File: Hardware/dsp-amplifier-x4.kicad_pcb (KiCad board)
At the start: 4 copper layers, 182 x 90 mm, 171 parts, among them J1 USBi, J10 Conn_Coaxial, J2 EXT, J3 Raspberry_Pi_2_3, J4 Screw_Terminal_01x02, J5 Screw_Terminal_01x02, J6 Screw_Terminal_01x02, J7 Screw_Terminal_01x02, J8 USB_B, J9 Conn_Coaxial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

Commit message: smallify
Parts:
- removed C28, C32: 100n, Capacitor_SMD:C_0603_1608Metric_Pad1.08x0.95mm_HandSolder
- removed C30, C34, C36, C38, C40: 10u, Capacitor_SMD:C_1206_3216Metric_Pad1.33x1.80mm_HandSolder
- removed L1: 10u, Inductor_SMD:L_Abracon_ASPI-0630LR
- removed R25: 511k, Resistor_SMD:R_0603_1608Metric_Pad0.98x0.95mm_HandSolder
- removed R26, R29: 100k, Resistor_SMD:R_0603_1608Metric_Pad0.98x0.95mm_HandSolder
- removed R30: 13.5k, Resistor_SMD:R_0603_1608Metric_Pad0.98x0.95mm_HandSolder
- removed U3: TPS54308, Package_TO_SOT_SMD:SOT-23-6
- moved U5 107.7 mm to (125.8, 49.8)
- moved C42 94.7 mm to (133.0, 51.0), turned to 0 degrees
- moved C37 71.6 mm to (139.5, 71.2), turned to 90 degrees
- moved C41 67.9 mm to (142.2, 71.2), turned to 90 degrees
- moved L2 66.1 mm to (146.5, 78.0), turned to 0 degrees
- moved C35 64.2 mm to (145.0, 71.2), turned to 90 degrees
- moved C39 60.5 mm to (147.8, 71.2), turned to 90 degrees
- moved C33 53.3 mm to (149.2, 66.5), turned to 90 degrees
- moved C29 52.9 mm to (153.5, 73.0), turned to 180 degrees
- moved U4 51.2 mm to (152.0, 66.5), turned to 90 degrees
- moved C31 49.9 mm to (154.0, 75.2), turned to 180 degrees
- moved R32 49.0 mm to (152.0, 63.5), turned to 180 degrees
- moved R31 48.6 mm to (152.0, 61.8), turned to 0 degrees
- moved R27 47.3 mm to (154.8, 66.5), turned to 90 degrees
- moved R28 46.1 mm to (154.8, 63.0), turned to 90 degrees
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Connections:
- J3 pad 2: +5VD -> +5VA
- J3 pad 4: +5VD -> +5VA
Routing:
- net +5VA: track 225.4 -> 26.2 mm, vias 5 -> 0
- net +5VD: track 27.4 -> 0.00 mm, vias 6 -> 0
- net GND: track 218.5 -> 192.1 mm, vias 114 -> 88
- net /PI_SDATA_O: track 72.8 -> 65.6 mm
- net Net-(C32-Pad1): track 7.00 -> 0.00 mm, vias 9 -> 0
- net Net-(R25-Pad2): track 5.96 -> 0.00 mm
- net /Power/FB_5V0: track 5.17 -> 0.00 mm
- net Net-(J3-Pad40): track 6.33 -> 10.9 mm
- net Net-(C32-Pad2): track 3.57 -> 0.00 mm
- net Net-(C33-Pad1): track 7.00 -> 3.91 mm, vias 9 -> 7
- net /PI_LRCLK: track 67.1 -> 64.3 mm
- net Net-(C33-Pad2): track 3.57 -> 1.90 mm
- net /Power/FB_5V0_SEC: track 5.17 -> 3.67 mm
- net +3.3VA: vias 18 -> 6
- added copper zone on In2.Cu, net +5VA
- removed copper zone on F.Cu, net +3.3VA
- removed copper zone on In2.Cu, net +3.3VA
- removed copper zone on F.Cu, net +5VD
- removed copper zone on In2.Cu, net +5VD
- removed copper zone on B.Cu, net Net-(C32-Pad1)
- removed copper zone on F.Cu, net Net-(C32-Pad1)
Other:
- board text added: "+5V"
- board text added: "+5V supplied"
- board text removed: "+3.3VA"
- board text removed: "+5VA"
- board text removed: "+5VA supplied"
- board text removed: "+5VD"
- board text removed: "DC/DC"

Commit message: slight adjustments
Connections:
- J3 pad 13: /PI_MUTE -> (no net)
- U1 pad 69: /PI_MUTE -> (no net)
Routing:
- net /PI_MUTE: track 58.1 -> 0.00 mm, vias 2 -> 0
- net (no net): track 0.00 -> 58.1 mm, vias 6 -> 8

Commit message: mostly ready
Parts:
- removed P1: Conn_WallPlug, terminal_connectors:wuerth_691216410002
- removed PS1: IRM-60-24, Converter_ACDC:Converter_ACDC_MeanWell_IRM-60-xx_THT
- added J11: Screw_Terminal_01x02, terminal_connectors:wuerth_691216410002, B.Cu at (172.0, 71.5)
- moved C42 17.0 mm to (123.0, 64.8), turned to 270 degrees
- moved U5 14.7 mm to (129.2, 64.0), turned to 180 degrees
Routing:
- net +5VA: track 26.2 -> 110.9 mm, vias 0 -> 13
- net /Power/AC_N: track 33.8 -> 0.00 mm
- net /Power/AC_L: track 21.7 -> 0.00 mm
- net GND: track 192.1 -> 192.4 mm, vias 88 -> 91
- net +3.3VA: vias 6 -> 10
- net (no net): vias 8 -> 6
- added copper zone on F.Cu, net +3.3VA
- added copper zone on In2.Cu, net +3.3VA
- removed copper zone on In2.Cu, net +24V
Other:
- board size 182 x 90 mm -> 121.2 x 90 mm
- board text removed: "!"
- board text removed: "0/0"
- board text removed: "0/80"
- board text removed: "108/76"
- board text removed: "172/0"
- board text removed: "172/80"
- board text removed: "80/0"
- board text removed: "AC"

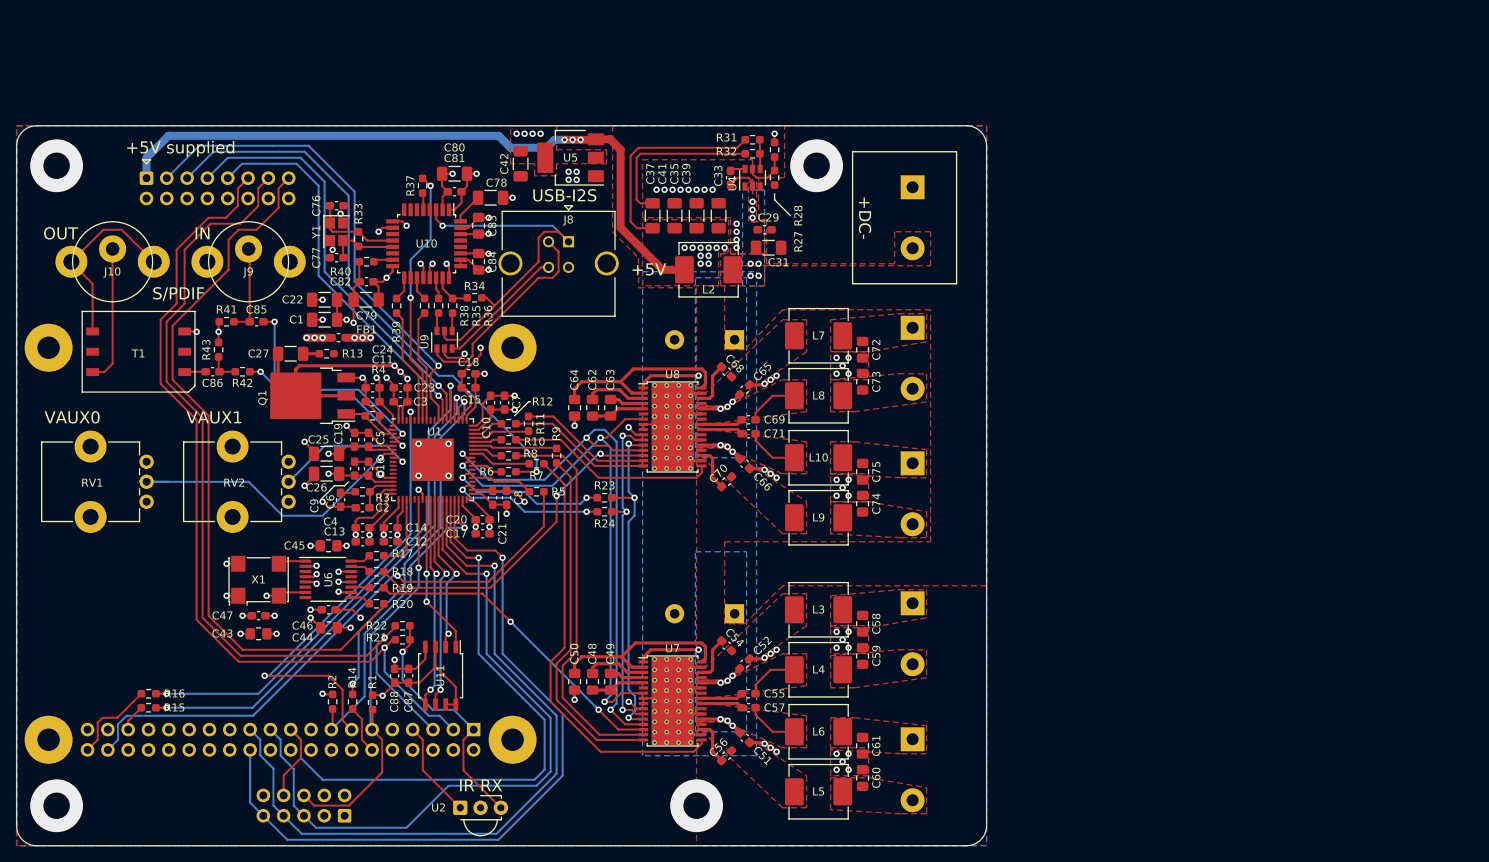
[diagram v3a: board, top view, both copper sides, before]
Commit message: feat: finalize layout for smaller blus
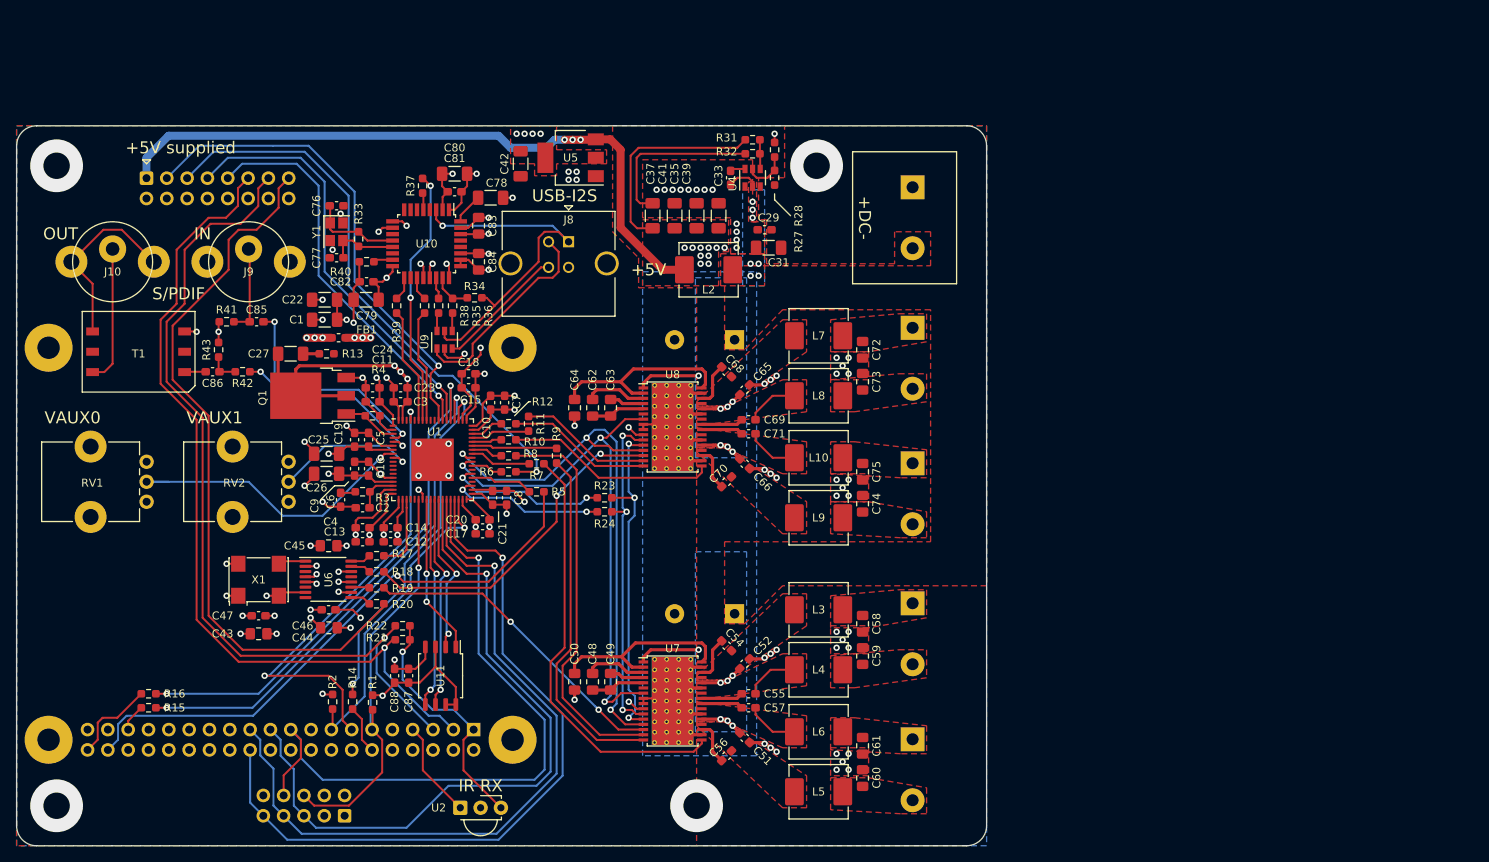
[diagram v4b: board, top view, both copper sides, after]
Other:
- net class Default removed
- board text added: "schwergängige poti montageöffnungen"

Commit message: Updated power supply
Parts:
- removed C37, C39, C41, C42: 10u, Capacitor_SMD:C_1206_3216Metric_Pad1.33x1.80mm_HandSolder
- removed L2: 10u, Inductor_SMD:L_Abracon_ASPI-0630LR
- removed R27: 511k, Resistor_SMD:R_0603_1608Metric_Pad0.98x0.95mm_HandSolder
- removed R28, R31: 100k, Resistor_SMD:R_0603_1608Metric_Pad0.98x0.95mm_HandSolder
- removed R32: 13.5k, Resistor_SMD:R_0603_1608Metric_Pad0.98x0.95mm_HandSolder
- removed U5: AMS1117-3.3, Package_TO_SOT_SMD:SOT-223-3_TabPin2
- added C28: 100n, Capacitor_SMD:C_0603_1608Metric_Pad1.08x0.95mm_HandSolder, F.Cu at (146.8, 74.0)
- added C30: 100n, Capacitor_SMD:C_0603_1608Metric_Pad1.08x0.95mm_HandSolder, F.Cu at (151.5, 71.2)
- added C32: 10u, Capacitor_SMD:C_1206_3216Metric_Pad1.33x1.80mm_HandSolder, F.Cu at (146.0, 65.0)
- added C34: 10u, Capacitor_SMD:C_1206_3216Metric_Pad1.33x1.80mm_HandSolder, F.Cu at (146.0, 62.5)
- added L1: 4.7u, Inductor_SMD:L_Abracon_ASPI-0630LR, F.Cu at (139.8, 71.0)
- added R25: 54.9k, Resistor_SMD:R_0603_1608Metric_Pad0.98x0.95mm_HandSolder, F.Cu at (154.6, 74.0)
- added R26: 10k, Resistor_SMD:R_0603_1608Metric_Pad0.98x0.95mm_HandSolder, F.Cu at (156.4, 74.0)
- added U3: TPS563200, Package_TO_SOT_SMD:SOT-23-6, F.Cu at (151.5, 74.0)
- C29, C33: value 100n -> 10u; footprint Capacitor_SMD:C_0603_1608Metric_Pad1.08x0.95mm_HandSolder -> Capacitor_SMD:C_1206_3216Metric_Pad1.33x1.80mm_HandSolder
- J11: moved to F.Cu
- U4: value TPS54308 -> AMS1117-3.3; footprint Package_TO_SOT_SMD:SOT-23-6 -> Package_TO_SOT_SMD:SOT-223-3_TabPin2
- moved C35 24.7 mm to (121.5, 63.5), turned to 180 degrees
- moved U4 22.9 mm to (129.2, 64.0), turned to 180 degrees
- moved C31 9.57 mm to (146.0, 70.0), turned to 0 degrees
- moved C29 8.81 mm to (144.8, 74.0), turned to 90 degrees
- moved C33 3.40 mm to (146.0, 67.5), turned to 0 degrees
- moved J11 0.06 mm to (172.0, 71.6)
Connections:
- C29 pad 1: +24V -> +15V
- C31 pad 1: +24V -> +5VA
- C33 pad 1: Net-(C33-Pad1) -> +5VA
- C33 pad 2: Net-(C33-Pad2) -> GND
- C35 pad 1: +5VA -> +3.3VA
- C51 pad 1: +24V -> +15V
- C52 pad 1: +24V -> +15V
- C53 pad 1: +24V -> +15V
- C65 pad 1: +24V -> +15V
- C66 pad 1: +24V -> +15V
- C67 pad 1: +24V -> +15V
- J1 pad 1: (no net) -> unconnected-(J1-Pad1)
- J1 pad 2: (no net) -> unconnected-(J1-Pad2)
- J1 pad 3: (no net) -> unconnected-(J1-Pad3)
- J1 pad 4: (no net) -> unconnected-(J1-Pad4)
- J11 pad 1: +24V -> +15V
- J3 pad 10: (no net) -> unconnected-(J3-Pad10)
- J3 pad 13: (no net) -> unconnected-(J3-Pad13)
- J3 pad 16: (no net) -> unconnected-(J3-Pad16)
- J3 pad 17: (no net) -> unconnected-(J3-Pad17)
- J3 pad 18: (no net) -> unconnected-(J3-Pad18)
- J3 pad 22: (no net) -> unconnected-(J3-Pad22)
- J3 pad 26: (no net) -> unconnected-(J3-Pad26)
- J3 pad 27: (no net) -> unconnected-(J3-Pad27)
- J3 pad 28: (no net) -> unconnected-(J3-Pad28)
- J3 pad 29: (no net) -> unconnected-(J3-Pad29)
- J3 pad 31: (no net) -> unconnected-(J3-Pad31)
- J3 pad 32: (no net) -> unconnected-(J3-Pad32)
- J3 pad 33: (no net) -> unconnected-(J3-Pad33)
- J3 pad 36: (no net) -> unconnected-(J3-Pad36)
- J3 pad 37: (no net) -> unconnected-(J3-Pad37)
- J3 pad 8: (no net) -> unconnected-(J3-Pad8)
- T1 pad 2: (no net) -> unconnected-(T1-Pad2)
- T1 pad 5: (no net) -> unconnected-(T1-Pad5)
- U1 pad 10: (no net) -> unconnected-(U1-Pad10)
- U1 pad 11: (no net) -> unconnected-(U1-Pad11)
- U1 pad 12: (no net) -> unconnected-(U1-Pad12)
- U1 pad 13: (no net) -> unconnected-(U1-Pad13)
- U1 pad 22: (no net) -> unconnected-(U1-Pad22)
- U1 pad 23: (no net) -> unconnected-(U1-Pad23)
- U1 pad 40: (no net) -> unconnected-(U1-Pad40)
- U1 pad 43: (no net) -> unconnected-(U1-Pad43)
- U1 pad 63: (no net) -> unconnected-(U1-Pad63)
- U1 pad 64: (no net) -> unconnected-(U1-Pad64)
- U1 pad 68: (no net) -> /AUX_BCLK
- U1 pad 69: (no net) -> /AUX_LRCLK
- U1 pad 70: (no net) -> /AUX_MDI
- U10 pad 11: (no net) -> /USB_SUSPEND
- U10 pad 14: (no net) -> unconnected-(U10-Pad14)
- U10 pad 18: (no net) -> unconnected-(U10-Pad18)
- U10 pad 28: (no net) -> unconnected-(U10-Pad28)
- U10 pad 29: (no net) -> unconnected-(U10-Pad29)
- U10 pad 4: (no net) -> unconnected-(U10-Pad4)
- U10 pad 6: (no net) -> unconnected-(U10-Pad6)
- U10 pad 7: (no net) -> unconnected-(U10-Pad7)
- U10 pad 8: (no net) -> unconnected-(U10-Pad8)
- U4 pad 2: Net-(C33-Pad1) -> +3.3VA
- U4 pad 3: +24V -> +5VA
- U6 pad 13: (no net) -> /Clock/CLK2
- U6 pad 3: (no net) -> /Clock/CLK0
- U6 pad 6: (no net) -> /Clock/CLK4
- U6 pad 8: (no net) -> /Clock/CLK6
- U7 pad 1: +24V -> +15V
- U7 pad 21: +24V -> +15V
- U7 pad 28: +24V -> +15V
- U7 pad 6: (no net) -> /I2S-AMP-2CH-A/NSPK_FAULT
- U8 pad 1: +24V -> +15V
- U8 pad 21: +24V -> +15V
- U8 pad 28: +24V -> +15V
- U8 pad 6: (no net) -> /I2S-AMP-2CH-B/NSPK_FAULT
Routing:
- net unconnected-(J3-Pad13): track 0.00 -> 58.1 mm, vias 0 -> 2
- net (no net): track 58.1 -> 0.00 mm, vias 6 -> 4
- net +24V: track 37.6 -> 0.00 mm, vias 14 -> 0
- net +15V: track 0.00 -> 37.6 mm, vias 0 -> 14
- net +5VA: track 110.9 -> 82.2 mm, vias 13 -> 3
- net GND: track 192.4 -> 173.8 mm, vias 91 -> 85
- net Net-(R27-Pad2): track 5.61 -> 0.00 mm
- net Net-(C33-Pad1): track 3.91 -> 0.00 mm, vias 7 -> 0
- net /Power-15V/FB_5V0: track 0.00 -> 3.77 mm
- net /Power/FB_5V0_SEC: track 3.67 -> 0.00 mm
- net Net-(U3-Pad6): track 0.00 -> 1.91 mm
- net Net-(C33-Pad2): track 1.90 -> 0.00 mm
- net Net-(U3-Pad2): track 0.00 -> 1.39 mm, vias 0 -> 9
- added copper zone on B.Cu, net +15V
- added copper zone on F.Cu, net +15V
- added copper zone on B.Cu, net Net-(U3-Pad2)
- added copper zone on F.Cu, net Net-(U3-Pad2)
- removed copper zone on B.Cu, net +24V
- removed copper zone on F.Cu, net +24V
- removed copper zone on B.Cu, net Net-(C33-Pad1)
- removed copper zone on F.Cu, net Net-(C33-Pad1)
